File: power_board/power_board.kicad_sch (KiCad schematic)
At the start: 6 parts, among them CN1 XT90PW-M.G.Y, CN2 XT60PW-M, U13 MR60PW-M.G.B

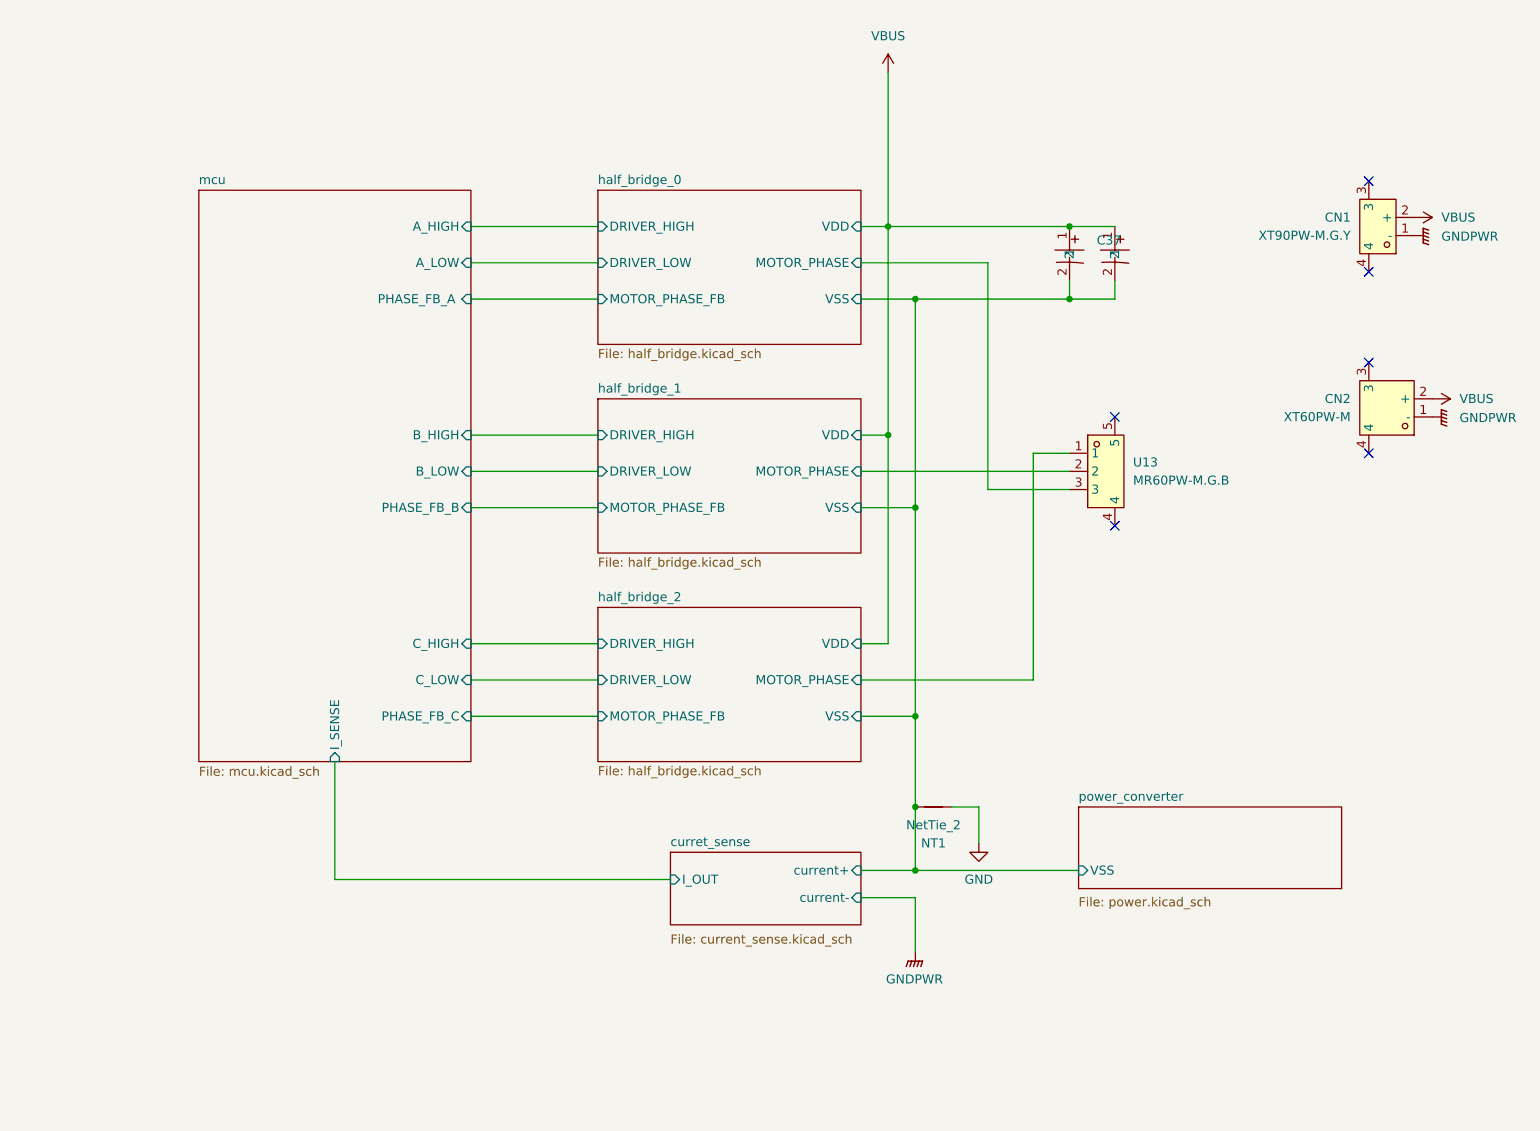
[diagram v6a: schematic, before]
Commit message: Add testpoint, SWD, and PWM port
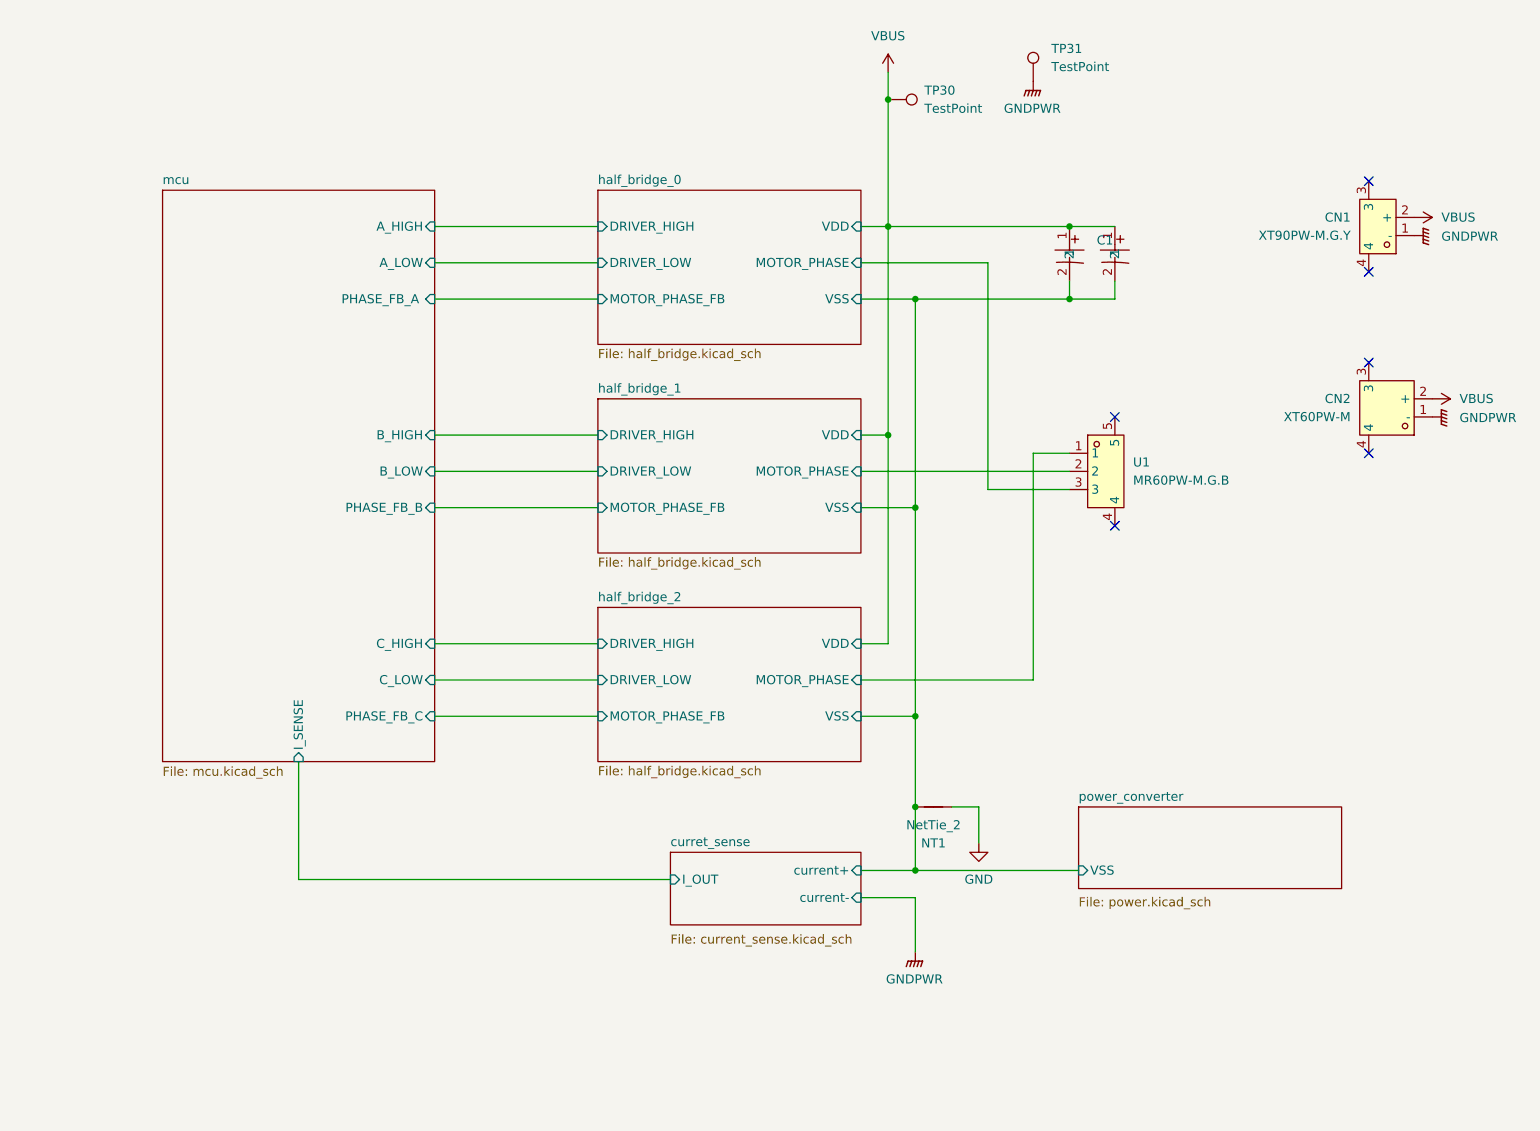
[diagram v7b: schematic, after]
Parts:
- added TP30, TP31: TestPoint, esc-library:SMD_RH-5015, symbol Connector:TestPoint
- renumbered C37 to C1, C38 to C2, U13 to U1
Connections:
- net GNDPWR: now also TP31.1
- net VBUS: now also TP30.1

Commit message: Add JLCJLCJLCJLC
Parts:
- added H1, H2: MountingHole_Pad, MountingHole:MountingHole_4.3mm_M4_Pad_Via, symbol Mechanical:MountingHole_Pad
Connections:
- no-connect marks 6 -> 8
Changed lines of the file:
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@@
+	)
+	(no_connect
+		(at 46.99 177.8)
 	)
 	(no_connect
@@
 	)
 	(no_connect
+		(at 38.1 177.8)
+	)
+	(no_connect
 		(at 209.55 74.93)
 	)
@@
 			(width 0)
 			(type default)
+		)
+	)
+	(symbol
+		(lib_id "Mechanical:MountingHole_Pad")
+		(at 46.99 175.26 0)
+		(unit 1)
+		(exclude_from_sim no)
+		(in_bom no)
+		(on_board yes)
+		(dnp no)
+		(fields_autoplaced yes)
+		(property "Reference" "H1"
+			(at 49.53 172.7199 0)
+			(effects
+				(font
+					(size 1.27 1.27)
+				)
+				(justify left)
+			)
+		)
+		(property "Value" "MountingHole_Pad"
+			(at 49.53 175.2599 0)
+			(effects
+				(font
+					(size 1.27 1.27)
+				)
+				(justify left)
+			)
+		)
+		(property "Footprint" "MountingHole:MountingHole_4.3mm_M4_Pad_Via"
+			(at 46.99 175.26 0)
+			(effects
+				(font
+					(size 1.27 1.27)
+				)
+				(hide yes)
+			)
+		)
+		(property "Datasheet" "~"
+			(at 46.99 175.26 0)
+			(effects
+				(font
+					(size 1.27 1.27)
+				)
+				(hide yes)
+			)
+		)
+		(property "Description" "Mounting Hole with connection"
+			(at 46.99 175.26 0)
+			(effects
+				(font
+					(size 1.27 1.27)
+				)
+				(hide yes)
+			)
+		)
+		(pin "1"
+		)
+		(instances
+			(project ""
+				(path "/c786dd1f-c97f-4c1e-a27a-ac5828b3c50c"
+					(reference "H1")
+					(unit 1)
+				)
+			)
 		)
 	)
@@
 					(unit 1)
 				)
+			)
+		)
+	)
+	(symbol
+		(lib_id "Mechanical:MountingHole_Pad")
+		(at 38.1 175.26 0)
+		(unit 1)
+		(exclude_from_sim no)
+		(in_bom no)
+		(on_board yes)
+		(dnp no)
+		(fields_autoplaced yes)
+		(property "Reference" "H2"
+			(at 40.64 172.7199 0)
+			(effects
+				(font
+					(size 1.27 1.27)
+				)
+				(justify left)
+			)
+		)
+		(property "Value" "MountingHole_Pad"
+			(at 40.64 175.2599 0)
+			(effects
+				(font
+					(size 1.27 1.27)
+				)
+				(justify left)
+			)
+		)
+		(property "Footprint" "MountingHole:MountingHole_4.3mm_M4_Pad_Via"
+			(at 38.1 175.26 0)
+			(effects
+				(font
+					(size 1.27 1.27)
+				)
+				(hide yes)
+			)
+		)
+		(property "Datasheet" "~"
+			(at 38.1 175.26 0)
+			(effects
+				(font
+					(size 1.27 1.27)
+				)
+				(hide yes)
+			)
+		)
+		(property "Description" "Mounting Hole with connection"
+			(at 38.1 175.26 0)
+			(effects
+				(font
+					(size 1.27 1.27)
+				)
+				(hide yes)
+			)
+		)
+		(pin "1"
+		)
+		(instances
+			(project "power_board"
+				(path "/c786dd1f-c97f-4c1e-a27a-ac5828b3c50c"
+					(reference "H2")
+					(unit 1)
+				)
